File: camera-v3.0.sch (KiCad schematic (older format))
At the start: 9 parts, among them IC1 USB2660I-JZX-03, J1 1775862-2, J2 104031-0811, J3 503960-0696, J4 1-1734742-6, J5 1734742-8, J6 53398-0867, U1 E73-2G4M08S1C-52840, U2 AXP209

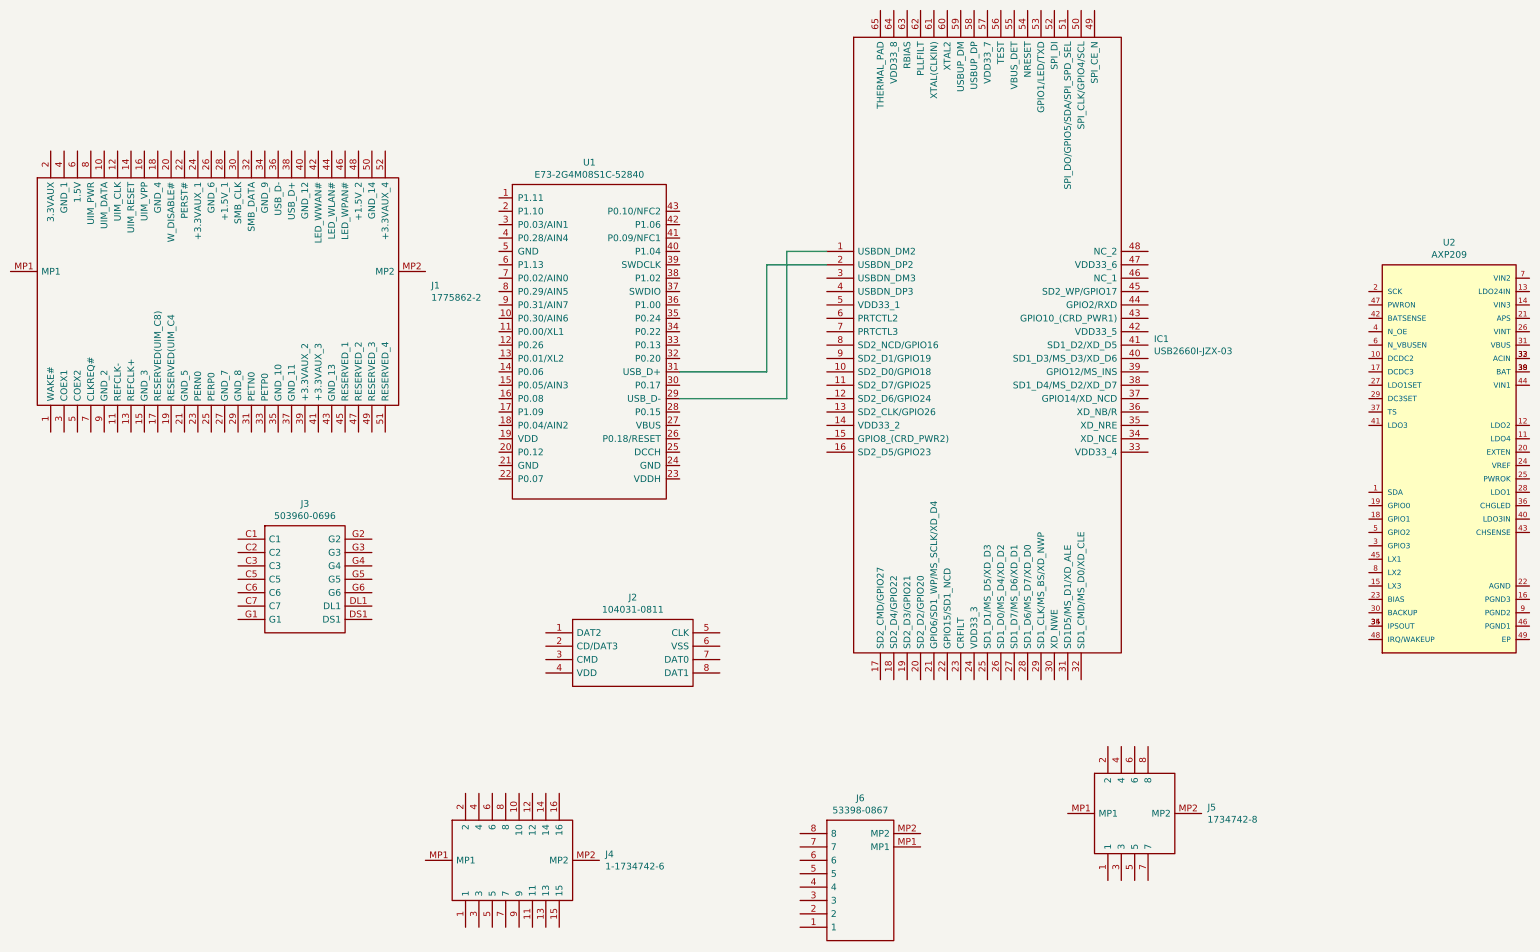
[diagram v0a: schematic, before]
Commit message: Заменены слоты SD и SIM на более дешевые
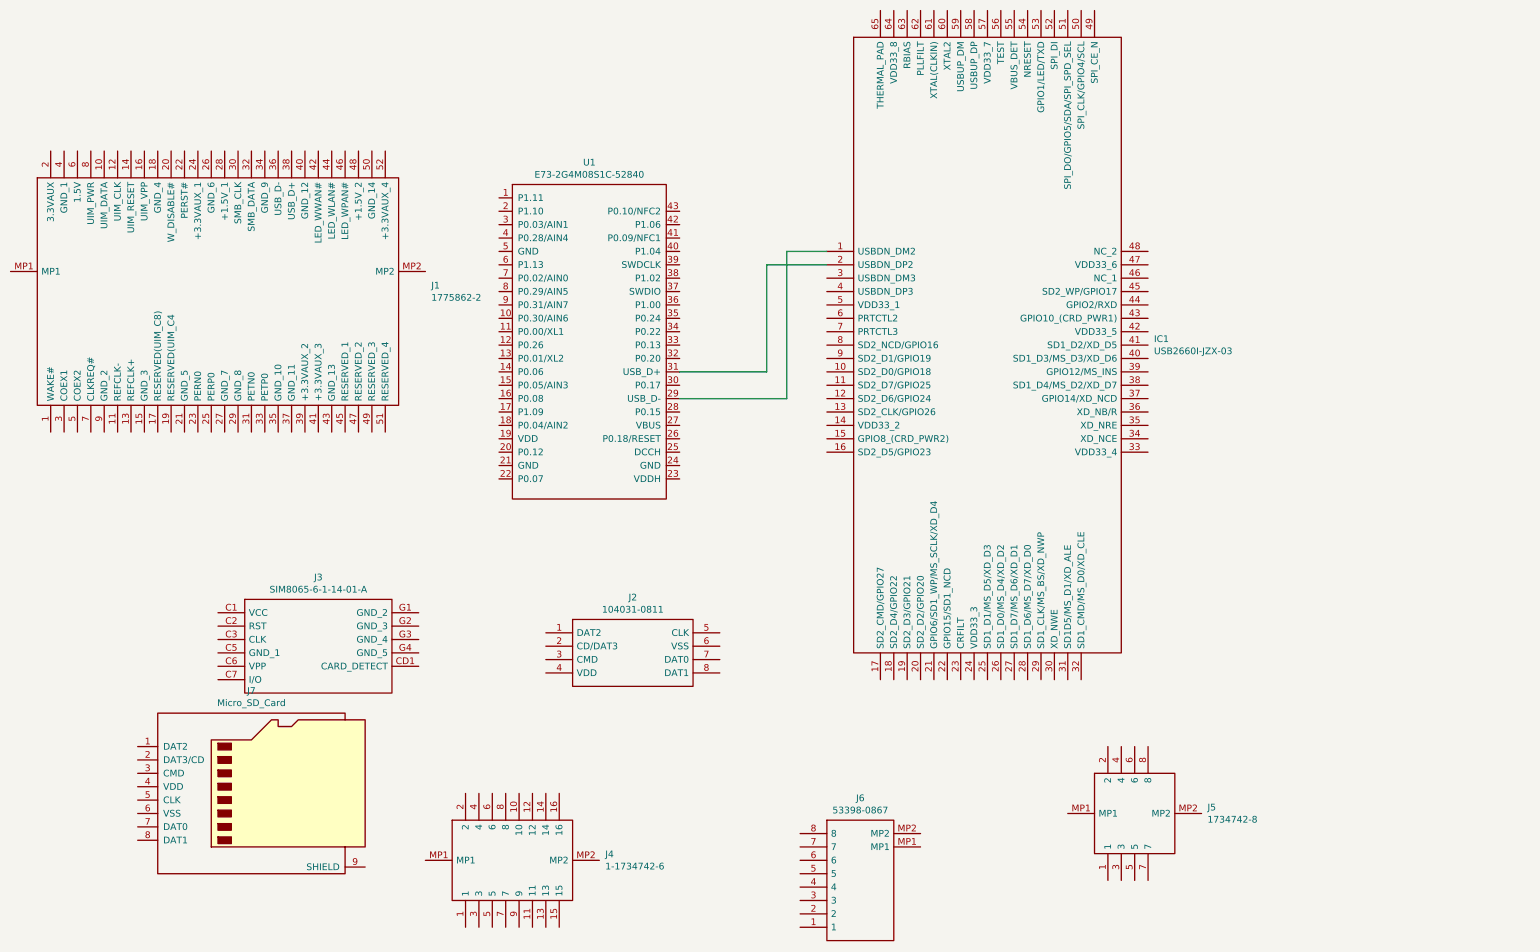
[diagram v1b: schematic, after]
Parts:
- removed J3: 503960-0696, mouser-local:5039600696, symbol camera-v3.0-rescue:503960-0696-mouser
- removed U2: AXP209, mouser-local:QFN40P600X600X80-49N, symbol mouser-local:AXP209
- added J3: SIM8065-6-1-14-01-A, SIM8065611401A, symbol mouser-local:SIM8065-6-1-14-01-A
- added J7: Micro_SD_Card, symbol Connector:Micro_SD_Card
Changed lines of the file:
@@
 	6850 2900 7300 2900
-$Comp
-L camera-v3.0-rescue:503960-0696-mouser J3
-U 1 1 6067DDEC
-P 2900 4950
-F 0 "J3" H 3400 5215 50  0000 C CNN
-F 1 "503960-0696" H 3400 5124 50  0000 C CNN
-F 2 "mouser-local:5039600696" H 3750 5050 50  0001 L CNN
-F 3 "https://www.molex.com/pdm_docs/sd/5039600696_sd.pdf" H 3750 4950 50  0001 L CNN
-F 4 "Memory Card Connectors 1mm microSIM Push Push SMT 6Ckt" H 3750 4850 50  0001 L CNN "Description"
-F 5 "1" H 3750 4750 50  0001 L CNN "Height"
-F 6 "538-503960-0696" H 3750 4650 50  0001 L CNN "Mouser Part Number"
-F 7 "https://www.mouser.co.uk/ProductDetail/Molex/503960-0696/?qs=c8NFF48pVsD9CCuzl855Ng%3D%3D" H 3750 4550 50  0001 L CNN "Mouser Price/Stock"
-F 8 "Molex" H 3750 4450 50  0001 L CNN "Manufacturer_Name"
-F 9 "503960-0696" H 3750 4350 50  0001 L CNN "Manufacturer_Part_Number"
-	1    2900 4950
-	1    0    0    -1
-$EndComp
-$Comp
-L mouser-local:AXP209 U2
-U 1 1 609E4991
-P 11950 4400
-F 0 "U2" H 11950 6067 50  0000 C CNN
-F 1 "AXP209" H 11950 5976 50  0000 C CNN
-F 2 "mouser-local:QFN40P600X600X80-49N" H 11950 4400 50  0001 L BNN
-F 3 "" H 11950 4400 50  0001 L BNN
-F 4 "X-Powers Limited" H 11950 4400 50  0001 L BNN "MANUFACTURER"
-	1    11950 4400
-	1    0    0    -1
-$EndComp
 $Comp
 L mouser-local:1-1734742-6 J4
@@
 	1    0    0    -1
 $EndComp
+$Comp
+L mouser-local:SIM8065-6-1-14-01-A J3
+U 1 1 60A7891A
+P 2750 5500
+F 0 "J3" H 3500 5765 50  0000 C CNN
+F 1 "SIM8065-6-1-14-01-A" H 3500 5674 50  0000 C CNN
+F 2 "SIM8065611401A" H 4100 5600 50  0001 L CNN
+F 3 "" H 4100 5500 50  0001 L CNN
+F 4 "NANO SIM PUSH-PUSH 6P 1.37MM H G" H 4100 5400 50  0001 L CNN "Description"
+F 5 "1.57" H 4100 5300 50  0001 L CNN "Height"
+F 6 "" H 4100 5200 50  0001 L CNN "Mouser Part Number"
+F 7 "" H 4100 5100 50  0001 L CNN "Mouser Price/Stock"
+F 8 "GCT (GLOBAL CONNECTOR TECHNOLOGY)" H 4100 5000 50  0001 L CNN "Manufacturer_Name"
+F 9 "SIM8065-6-1-14-01-A" H 4100 4900 50  0001 L CNN "Manufacturer_Part_Number"
+	1    2750 5500
+	1    0    0    -1
+$EndComp
+$Comp
+L Connector:Micro_SD_Card J7
+U 1 1 60A79CAE
+P 3050 6800
+F 0 "J7" H 3000 7517 50  0000 C CNN
+F 1 "Micro_SD_Card" H 3000 7426 50  0000 C CNN
+F 2 "" H 4200 7100 50  0001 C CNN
+F 3 "http://katalog.we-online.de/em/datasheet/693072010801.pdf" H 3050 6800 50  0001 C CNN
+	1    3050 6800
+	1    0    0    -1
+$EndComp
